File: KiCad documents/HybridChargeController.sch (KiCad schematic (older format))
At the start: 23 parts

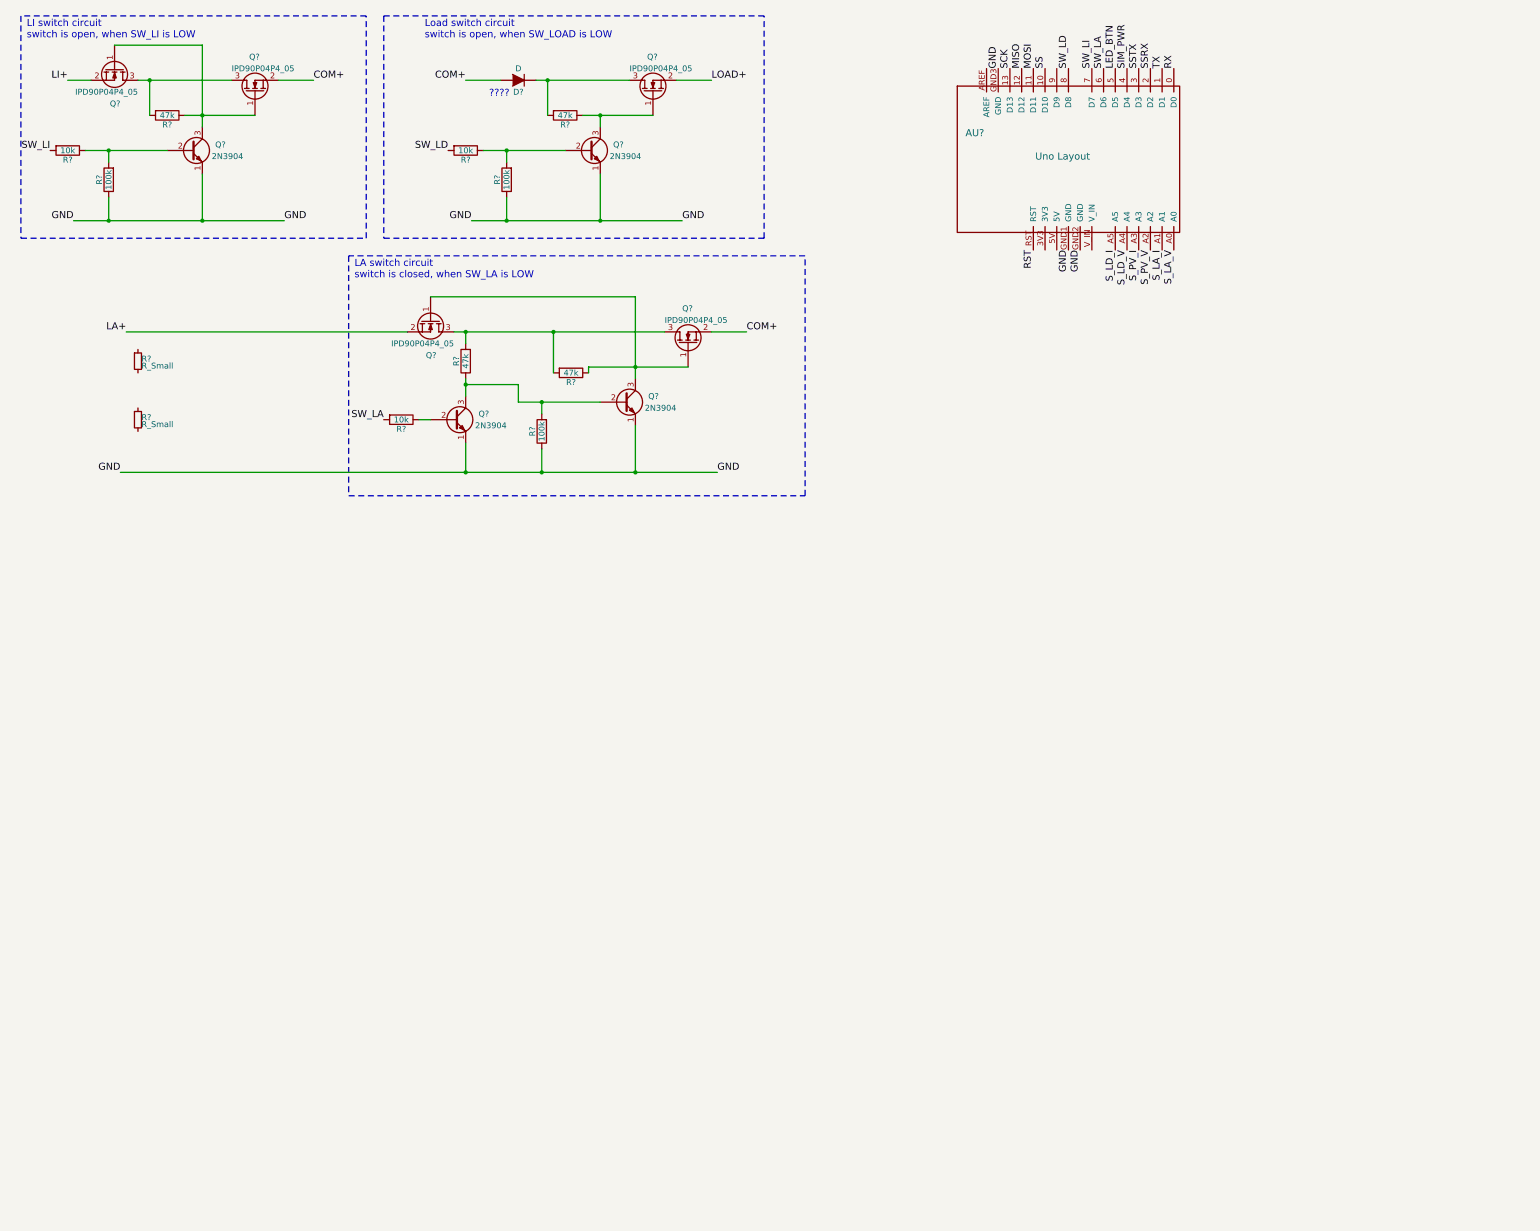
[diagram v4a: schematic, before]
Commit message: added vcs PV and connectors
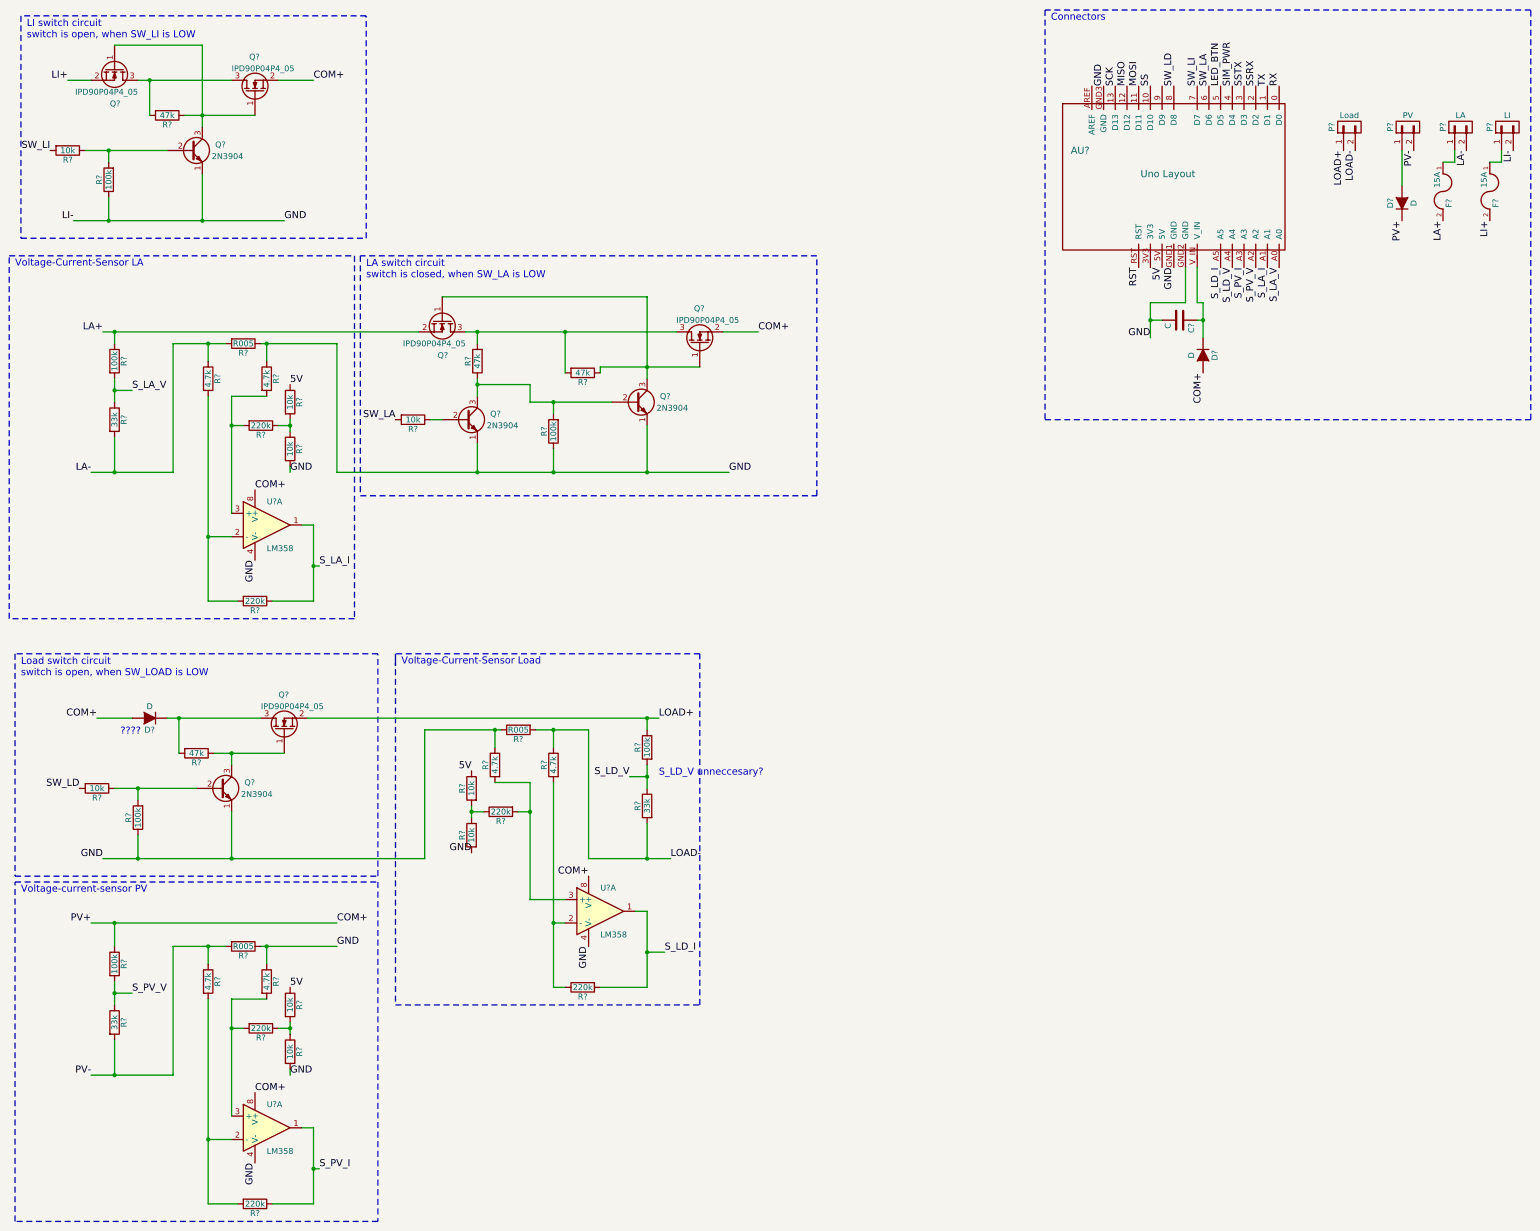
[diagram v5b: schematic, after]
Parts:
- removed R? (x2): R_Small, symbol R_Small
- added C?: C, symbol C
- added D? (x2): D, symbol D
- added F? (x2): 15A, symbol FUSE
- added P?: Load, symbol CONN_01X02
- added P?: PV, symbol CONN_01X02
- added P?: LA, symbol CONN_01X02
- added P?: LI, symbol CONN_01X02
- added R? (x3): 33k, symbol R
- added R? (x3): 100k, symbol R
- added R? (x3): R005, symbol R
- added R? (x6): 4.7k, symbol R
- added R? (x6): 10k, symbol R
- added R? (x6): 220k, symbol R
- added U? (x3): LM358, symbol LM358
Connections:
- net COM+: now also D?.1 (K), D?.2 (A), R?.1, U?.8 (V+), U?.8 (V+), U?.8 (V+)
- net GND: now also C?.2, P?.2 (P2), R?.1, R?.1, R?.1, R?.1, R?.1, R?.1, R?.2, R?.2, R?.2, U?.4 (V-), U?.4 (V-), U?.4 (V-)
- net LA+: now also F?.2, R?.1
- net LI+: now also F?.2
- net LOAD+: now also P?.1 (P1), R?.1
- net S_LA_I: now also R?.1, U?.1
- net S_LA_V: now also R?.1, R?.2
- net S_LD_I: now also R?.2, U?.1
- net S_LD_V: now also R?.1, R?.2
- net S_PV_I: now also R?.1, U?.1
- net S_PV_V: now also R?.1, R?.2
- net 5V: now reaches AU?.5V
- net 5V: now also R?.1, R?.1, R?.1
- net at AU?.V_IN: now also C?.1, D?.1 (K)
- new net: R?.2, R?.2, U?.2 (-) (x2)
- new net: R?.2, R?.2, U?.3 (+) (x3)
- new net: R?.1, R?.1, R?.2 (x3)
- new net: F?.1, P?.1 (P1) (x2)
- new net: R?.1, R?.2, U?.2 (-)
- new net: D?.2 (A), P?.1 (P1)
- new net LA-: P?.2 (P2), R?.1, R?.2, R?.2
- new net LOAD-: P?.2 (P2), R?.1, R?.2, R?.2
- new net PV-: P?.2 (P2), R?.1, R?.2, R?.2
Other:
- note added: "Connectors"
- note added: "S_LD_V unneccesary?"
- note added: "Voltage-Current-Sensor LA"
- note added: "Voltage-Current-Sensor Load"
- note added: "Voltage-current-sensor PV"
- moved on the sheet: AU?, D?, Q?, R?

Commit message: no changes?
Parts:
- removed R?: 33k, symbol R
- removed R?: 100k, symbol R
- added D?: D, symbol D
- added Q?: 2N3904, symbol Q_NPN_EBC
- added Q?: IPD90P04P4_05, symbol Q_NMOS_GSD
- added R?: 2.2k, symbol R
- added R?: 100k, symbol R
- added R?: 10k, symbol R
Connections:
- net S_LD_V is gone; now on net S_LD_I: AU?.A4
- net COM+: now also D?.2 (A), Q?.2 (S)
- net PV-: now also Q?.1 (E), R?.1
- net S_LD_I: no longer AU?.A5
- new net: Q?.1 (G), Q?.3 (C), R?.1
- new net: D?.1 (K), Q?.3 (D), R?.2
- new net: Q?.2 (B), R?.1, R?.2
- new net SW_PV: R?.2
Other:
- note added: "PV switch circuit \nswitch is open, when SW_PV is LOW"
- note added: "This R needs to be low. 47k doesnt work"
- note removed: "S_LD_V unneccesary?"
- moved on the sheet: R?, U?A

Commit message: added only some comments and open questions for discussion
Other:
- note added: "(Voltage)-Current-Sensor Load"
- note added: "15A too big for LI?"
- note added: "I_Q = 1mA"
- note added: "LI = Li-Ion\nLA = Lead-Acid"
- note added: "Schottky? Mosfet? Nothing?"
- note added: "add a thermal fuse physically close to the lifepo?\n"
- note added: "how big? elko? footprint? ;-)"
- note added: "make this a Schottky"
- note added: "no voltage/current sensor for LI?"
- note added: "open:\n- reverse polarity all ports?\n- short-circuit protection all ports?\n- overvoltage?"
- note added: "sized for which max. current?"
- note added: "whats the max. switching freuqency possible here? \nIt will have to apply PWM charge-controlling?"
- note added: "where is the LiFePo-IC?"
- note removed: "Voltage-Current-Sensor Load"
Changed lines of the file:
@@
 $EndComp
 Text Notes 4000 6100 0    60   ~ 0
-Voltage-Current-Sensor Load
+(Voltage)-Current-Sensor Load
 $Comp
 L C C?
@@
 Text Notes 7300 7000 0    60   ~ 0
 This R needs to be low. 47k doesnt work
+Text Notes 700  11050 0    139  ~ 28
+LI = Li-Ion\nLA = Lead-Acid
+Text Notes 13650 1850 0    60   Italic 0
+15A too big for LI?
+Text Notes 12400 2200 3    60   Italic 0
+make this a Schottky
+Text Notes 13400 2400 0    60   Italic 0
+add a thermal fuse physically  close to the lifepo?\n
+Text Notes 2150 3100 0    60   Italic 0
+sized for which max. current?
+Text Notes 3000 4800 0    60   Italic 0
+I_Q = 1mA
+Text Notes 5800 8100 0    60   Italic 0
+I_Q = 1mA
+Text Notes 6300 4200 0    60   Italic 0
+whats the max. switching freuqency possible here? \nIt will  have to apply PWM charge-controlling?
+Text Notes 1500 6500 0    60   Italic 0
+Schottky? Mosfet? Nothing?
+Text Notes 7650 10950 0    139  Italic 0
+open:\n- reverse polarity all ports?\n- short-circuit protection all ports?\n- overvoltage?
+Text Notes 13000 7000 0    99   Italic 0
+where is the LiFePo-IC?
+Text Notes 10600 3350 0    60   Italic 0
+how big? elko? footprint? ;-)
+Text Notes 4150 1550 0    60   Italic 0
+no voltage/current sensor for LI?
 $EndSCHEMATC

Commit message: added LI IC, removed own LI circuit part
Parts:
- removed Q?: 2N3904, symbol Q_NPN_EBC
- removed Q? (x2): IPD90P04P4_05, symbol Q_NMOS_GSD
- removed R?: 47k, symbol R
- removed R?: 100k, symbol R
- removed R?: 10k, symbol R
- added C? (x4): Cc, symbol C_Small
- added C? (x2): 1µ, symbol C_Small
- added C?: Cf, symbol C_Small
- added C? (x3): 0,1µ, symbol C_Small
- added D?: ZENER, symbol ZENER
- added D?: D, symbol D
- added P?: LI_balancer, symbol CONN_01X03
- added Q? (x2): P FET, symbol Q_NMOS_DGS
- added Q?: N FET cheap, symbol Q_NMOS_DGS
- added R? (x5): Rc, symbol R
- added R?: Rsns, symbol R
- added R? (x3): 1M, symbol R
- added R?: Rf, symbol R
- added R? (x2): 10k, symbol R
- added R? (x2): 100, symbol R
- added U?: bq76920, symbol bq76920
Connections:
- net SW_LI is gone; now on net SW_LD: AU?.7 (D7)
- net GND: now also C?.2, C?.2, C?.2, C?.2, C?.2, D?.2 (A), Q?.2 (G), Q?.3 (S), R?.2, R?.2, U?.3 (VSS); no longer P?.2 (P2)
- net LI+: now also C?.1, R?.2, R?.2, U?.9 (REGSRC)
- net SW_LD: no longer AU?.8 (D8)
- net S_LA_I: no longer AU?.A1
- net S_LA_V: no longer AU?.A0
- net S_LD_I: no longer AU?.A4
- net S_PV_I: no longer AU?.A3
- net S_PV_V: no longer AU?.A2
- net SCL: now reaches AU?.A5
- net SCL: now also U?.5 (SCL)
- new net: C?.1, R?.1, U?.10 (BAT)
- new net: R?.1, R?.1, U?.6 (TS1)
- new net: C?.1, U?.7 (CAP1)
- new net: Q?.3 (S), R?.1, R?.1, R?.2
- new net: Q?.1 (D), Q?.1 (D)
- new net: D?.1 (K), D?.1 (K), Q?.2 (G), R?.1, R?.2
- new net: D?.2 (A), Q?.3 (S), R?.1
- new net Alert: U?.20 (ALERT)
- new net CELL12: R?.2
- new net CELL23: R?.2
- new net CELL34: R?.2
- new net CHG: Q?.1 (D), U?.2 (CHG)
- new net Cell12: P?.1 (P1)
- new net Cell23: P?.2 (P2)
- new net Cell34: P?.3 (P3)
- new net DSG: Q?.2 (G), R?.1, U?.1 (DSG)
- new net LI-: P?.2 (P2), R?.1, R?.2, R?.2
- new net SDA: AU?.A4, U?.4 (SDA)
- new net SRN: C?.1, C?.1, R?.2, U?.19 (SRN)
- new net SRP: C?.1, C?.2, R?.2, U?.18 (SRP)
- new net VC0: C?.2, R?.1, U?.17 (VC0)
- new net VC1: C?.1, C?.2, R?.1, R?.2, U?.16 (VC1)
- new net VC2: C?.1, C?.2, R?.1, U?.15 (VC2)
- new net VC3: C?.1, C?.2, R?.1, U?.13 (VC4), U?.14 (VC3)
- new net VC5: C?.1, R?.1, U?.12 (VC5)
- no-connect marks 0 -> 1
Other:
- note added: "Current-Sensor Load"
- note added: "LI (dis-)charge, balance, monitor IC"
- note added: "SIZE?\nRf, Cf"
- note added: "Zener maybe not needed? DATASHEET"
- note removed: "(Voltage)-Current-Sensor Load"
- note removed: "LI switch circuit \nswitch is open, when SW_LI is LOW"
- note removed: "no voltage/current sensor for LI?"
- note removed: "where is the LiFePo-IC?"
- moved on the sheet: AU?, C?, D?, F?, P?, Q?, R?, U?A
